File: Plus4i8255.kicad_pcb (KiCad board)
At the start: 2 copper layers, 52.1 x 70 mm, 13 parts, among them CN1 EXPANSION_PORT, CN3 PIN_HEADER_32PIN, U1 8255, U2 GAL20V8

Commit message: TurboFloppy -> Plus4i8255
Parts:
- CN1: footprint TurboFloppy:C16_Cart_Conn -> Plus4i8255:C16_Cart_Conn
- V0: footprint TurboFloppy:cc_by_nc_sa -> Plus4i8255:cc_by_nc_sa
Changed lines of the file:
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@@
 		(property ki_fp_filters "R?Array?SIP*")
 		(sheetname "Root")
-		(sheetfile "TurboFloppy.kicad_sch")
+		(sheetfile "Plus4i8255.kicad_sch")
 		(attr through_hole)
 		(fp_line
@@
 		(property ki_fp_filters "MountingHole*Pad*")
 		(sheetname "Root")
-		(sheetfile "TurboFloppy.kicad_sch")
+		(sheetfile "Plus4i8255.kicad_sch")
 		(zone_connect 2)
 		(attr exclude_from_pos_files exclude_from_bom)
@@
 		(property ki_fp_filters "DIP*W15.24mm* PDIP*W15.24mm*")
 		(sheetname "Root")
-		(sheetfile "TurboFloppy.kicad_sch")
+		(sheetfile "Plus4i8255.kicad_sch")
 		(attr through_hole)
 		(fp_line
@@
 		(property ki_fp_filters "R?Array?SIP*")
 		(sheetname "Root")
-		(sheetfile "TurboFloppy.kicad_sch")
+		(sheetfile "Plus4i8255.kicad_sch")
 		(attr through_hole)
 		(fp_line
@@
 		(property ki_fp_filters "MountingHole*Pad*")
 		(sheetname "Root")
-		(sheetfile "TurboFloppy.kicad_sch")
+		(sheetfile "Plus4i8255.kicad_sch")
 		(zone_connect 2)
 		(attr exclude_from_pos_files exclude_from_bom)
@@
 		(property ki_fp_filters "R?Array?SIP*")
 		(sheetname "Root")
-		(sheetfile "TurboFloppy.kicad_sch")
+		(sheetfile "Plus4i8255.kicad_sch")
 		(attr through_hole)
 		(fp_line
@@
 		(property ki_fp_filters "DIP* PDIP*")
 		(sheetname "Root")
-		(sheetfile "TurboFloppy.kicad_sch")
+		(sheetfile "Plus4i8255.kicad_sch")
 		(attr through_hole)
 		(fp_line
@@
 		(property ki_fp_filters "C_*")
 		(sheetname "Root")
-		(sheetfile "TurboFloppy.kicad_sch")
+		(sheetfile "Plus4i8255.kicad_sch")
 		(attr through_hole)
 		(fp_line
@@
 		(property ki_fp_filters "C_*")
 		(sheetname "Root")
-		(sheetfile "TurboFloppy.kicad_sch")
+		(sheetfile "Plus4i8255.kicad_sch")
 		(attr through_hole)
 		(fp_line
@@
 		)
 	)
-	(footprint "TurboFloppy:C16_Cart_Conn"
+	(footprint "Plus4i8255:C16_Cart_Conn"
 		(layer "F.Cu")
 		(at 146.053 132.588)
@@
 			)
 		)
-		(property "Footprint" "TurboFloppy:C16_Cart_Conn"
+		(property "Footprint" "Plus4i8255:C16_Cart_Conn"
 			(at 0 0 0)
 			(layer "F.Fab")
@@
 		)
 		(sheetname "Root")
-		(sheetfile "TurboFloppy.kicad_sch")
+		(sheetfile "Plus4i8255.kicad_sch")
 		(zone_connect 2)
 		(attr through_hole)
@@
 		(property ki_fp_filters "Connector*:*_2x??_*")
 		(sheetname "Root")
-		(sheetfile "TurboFloppy.kicad_sch")
+		(sheetfile "Plus4i8255.kicad_sch")
 		(attr through_hole)
 		(fp_line
@@
 		(property ki_fp_filters "CP_*")
 		(sheetname "Root")
-		(sheetfile "TurboFloppy.kicad_sch")
+		(sheetfile "Plus4i8255.kicad_sch")
 		(attr through_hole)
 		(fp_line
@@
 		)
 	)
-	(footprint "TurboFloppy:cc_by_nc_sa"
+	(footprint "Plus4i8255:cc_by_nc_sa"
 		(layer "B.Cu")
 		(at 161.925 125.222 180)
@@
 			)
 		)
-		(property "Footprint" "TurboFloppy:cc_by_nc_sa"
+		(property "Footprint" "Plus4i8255:cc_by_nc_sa"
 			(at 0 0 0)
 			(layer "B.Fab")
@@
 		)
 		(sheetname "Root")
-		(sheetfile "TurboFloppy.kicad_sch")
+		(sheetfile "Plus4i8255.kicad_sch")
 		(attr through_hole)
 		(fp_poly

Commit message: Add PC-style DB25 parallel port Inspired by zx_spectrum_parallel_interface by @msolajic TBD: Check DB25 footprint!
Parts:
- added C3: 100n, Capacitor_THT:C_Disc_D7.0mm_W2.5mm_P5.00mm, F.Cu at (135.9, 92.0)
- added CN2: PC_PARALLEL, Connector_Dsub:DSUB-25_Female_Horizontal_P2.77x2.84mm_EdgePinOffset7.70mm_Housed_MountingHolesOffset9.12mm, F.Cu at (129.4, 64.0)
- added JP1: JMP_PARPWR, Jumper:SolderJumper-2_P1.3mm_Open_RoundedPad1.0x1.5mm, B.Cu at (130.2, 58.5)
- added JP2: JMP_SELPRNT, Jumper:SolderJumper-2_P1.3mm_Open_RoundedPad1.0x1.5mm, B.Cu at (138.5, 58.5)
- added U3: 74HCT04, Package_DIP:DIP-14_W7.62mm_Socket_LongPads, F.Cu at (139.7, 98.3)
- renumbered C3 to C4
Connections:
- RN1 pad 2: /pb7 -> /pb5
- RN1 pad 4: /pb5 -> /pb7
- U2 pad 1: /~{reset} -> unconnected-(U2-I1-Pad1)
- U2 pad 17: /reset -> unconnected-(U2-IO17-Pad17)
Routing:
- net /~{strobe}: track 0.00 -> 69.6 mm, vias 0 -> 2
- net +5V: track 114.5 -> 166.5 mm, vias 1 -> 4
- net /pb7: track 59.6 -> 86.7 mm, vias 2 -> 3
- net /pc3: track 32.1 -> 55.8 mm, vias 0 -> 1
- net /pb6: track 61.5 -> 79.2 mm, vias 0 -> 1
- net /reset: track 25.3 -> 11.5 mm, vias 1 -> 0
- net /~{reset}: track 70.0 -> 82.0 mm, vias 2 -> 3
- net /pb0: track 13.0 -> 24.9 mm
- net /pb4: track 69.5 -> 81.3 mm, vias 1 -> 2
- net /pb1: track 19.7 -> 31.4 mm
- net /pb2: track 25.3 -> 36.9 mm
- net /pc7: track 36.0 -> 46.1 mm
- net /pb5: track 72.9 -> 82.4 mm, vias 2 -> 3
- net /pb3: track 50.6 -> 59.1 mm
- net /~{wr8255}: track 29.8 -> 34.6 mm
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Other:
- board size 52.1 x 70 mm -> 53.3 x 83.2 mm
- board text added: "PC-STYLE PARALLEL PORT"
- board text added: "PIN 14 +5V"
- board text added: "PIN 17 SELECT PRINTER"

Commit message: Move some tracks around
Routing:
- net /pb5: track 82.4 -> 79.4 mm
- net /~{rd8255}: track 43.6 -> 40.9 mm
- net /~{wr8255}: track 34.6 -> 32.2 mm
- net /a1: track 57.3 -> 58.8 mm
- net /a0: track 63.4 -> 63.9 mm

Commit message: Again
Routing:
- net /a0: track 63.9 -> 66.9 mm
- net /a1: track 58.8 -> 61.6 mm
- net /~{wr8255}: track 32.2 -> 34.9 mm, vias 1 -> 2
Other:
- outline, holes or cut-outs redrawn
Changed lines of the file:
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@@
 	(gr_line
 		(start 172.72 53.467)
-		(end 172.72 128.016)
+		(end 172.72 127.381)
 		(stroke
 			(width 0.05)
@@
 	(gr_line
 		(start 120.015 135.89)
-		(end 120.015 128.651)
+		(end 120.015 128.016)
 		(stroke
 			(width 0.05)
@@
 	)
 	(gr_arc
-		(start 172.72 128.016)
-		(mid 172.534013 128.465013)
-		(end 172.085 128.651)
+		(start 172.72 127.381)
+		(mid 172.534013 127.830013)
+		(end 172.085 128.016)
 		(stroke
 			(width 0.05)
@@
 	)
 	(gr_arc
-		(start 120.015 128.651)
-		(mid 119.565987 128.465013)
-		(end 119.38 128.016)
+		(start 120.015 128.016)
+		(mid 119.565987 127.830013)
+		(end 119.38 127.381)
 		(stroke
 			(width 0.05)
@@
 	(gr_line
 		(start 172.085 135.89)
-		(end 172.085 128.651)
+		(end 172.085 128.016)
 		(stroke
 			(width 0.05)
@@
 	)
 	(gr_line
-		(start 119.38 128.016)
+		(start 119.38 127.381)
 		(end 119.38 53.467)
 		(stroke
@@
 	)
 	(segment
-		(start 167.005 116.205)
+		(start 168.91 106.553)
 		(end 167.005 108.458)
 		(width 0.25)
@@
 	)
 	(segment
-		(start 149.86 86.868)
-		(end 151.129998 88.137998)
+		(start 167.005 108.458)
+		(end 167.005 116.205)
 		(width 0.25)
 		(layer "F.Cu")
@@
 	)
 	(segment
-		(start 168.91 106.553)
-		(end 168.91 100.33)
+		(start 149.86 86.868)
+		(end 149.86 88.392)
 		(width 0.25)
 		(layer "F.Cu")
@@
 	)
 	(segment
-		(start 167.005 108.458)
+		(start 168.91 95.25)
 		(end 168.91 106.553)
 		(width 0.25)
@@
 	)
 	(segment
-		(start 151.129998 88.137998)
+		(start 151.129998 89.661998)
 		(end 151.129998 95.25)
 		(width 0.25)
@@
 		(net 4)
 	)
+	(segment
+		(start 149.86 88.392)
+		(end 151.129998 89.661998)
+		(width 0.25)
+		(layer "F.Cu")
+		(net 4)
+	)
 	(via
 		(at 151.129998 95.25)
@@
 	)
 	(via
-		(at 168.91 100.33)
+		(at 168.91 95.25)
 		(size 0.6)
 		(drill 0.4)
@@
 	)
 	(segment
-		(start 168.91 100.33)
-		(end 160.782 100.33)
-		(width 0.25)
-		(layer "B.Cu")
-		(net 4)
-	)
-	(segment
-		(start 160.782 100.33)
-		(end 155.702 95.25)
-		(width 0.25)
-		(layer "B.Cu")
-		(net 4)
-	)
-	(segment
-		(start 155.702 95.25)
+		(start 168.91 95.25)
 		(end 151.129998 95.25)
 		(width 0.25)
@@
 	)
 	(segment
-		(start 153.669996 88.137996)
-		(end 153.669996 93.091)
-		(width 0.25)
-		(layer "F.Cu")
-		(net 11)
-	)
-	(segment
-		(start 152.4 86.868)
-		(end 153.669996 88.137996)
+		(start 166.37 115.569996)
+		(end 166.369996 115.57)
 		(width 0.25)
 		(layer "F.Cu")
@@
 	)
 	(segment
-		(start 153.67 93.091004)
-		(end 153.669996 93.091)
+		(start 166.37 94.615)
+		(end 166.37 115.569996)
 		(width 0.25)
 		(layer "F.Cu")
@@
 	)
 	(segment
-		(start 153.669996 93.091)
-		(end 153.669996 93.345)
+		(start 153.67 89.662)
+		(end 152.4 88.392)
 		(width 0.25)
 		(layer "F.Cu")
@@
 	(segment
 		(start 153.67 94.615)
-		(end 153.67 93.091004)
+		(end 153.67 89.662)
 		(width 0.25)
 		(layer "F.Cu")
@@
 	)
 	(segment
-		(start 166.37 99.695)
-		(end 166.37 115.569996)
-		(width 0.25)
-		(layer "F.Cu")
-		(net 11)
-	)
-	(segment
-		(start 166.37 115.569996)
-		(end 166.369996 115.57)
+		(start 152.4 88.392)
+		(end 152.4 86.868)
 		(width 0.25)
 		(layer "F.Cu")
@@
 	)
 	(via
-		(at 166.37 99.695)
+		(at 166.37 94.615)
 		(size 0.6)
 		(drill 0.4)
@@
 	)
 	(segment
-		(start 156.083 94.615)
-		(end 153.67 94.615)
-		(width 0.25)
-		(layer "B.Cu")
-		(net 11)
-	)
-	(segment
 		(start 160.053 132.588)
 		(end 160.053 121.886996)
@@
 	)
 	(segment
-		(start 166.37 99.695)
-		(end 161.163 99.695)
-		(width 0.25)
-		(layer "B.Cu")
-		(net 11)
-	)
-	(segment
-		(start 156.972 95.504)
-		(end 156.083 94.615)
-		(width 0.25)
-		(layer "B.Cu")
-		(net 11)
-	)
-	(segment
-		(start 161.163 99.695)
-		(end 156.972 95.504)
+		(start 160.053 121.886996)
+		(end 166.369996 115.57)
 		(width 0.25)
 		(layer "B.Cu")
@@
 	)
 	(segment
-		(start 160.053 121.886996)
-		(end 166.369996 115.57)
+		(start 166.37 94.615)
+		(end 153.67 94.615)
 		(width 0.25)
 		(layer "B.Cu")
@@
 	)
 	(segment
+		(start 160.02 95.885)
+		(end 160.02 102.108)
+		(width 0.25)
+		(layer "F.Cu")
+		(net 72)
+	)
+	(segment
 		(start 147.955 105.156)
 		(end 147.955 107.061)
@@
 		(net 72)
 	)
-	(segment
-		(start 146.05 95.885)
-		(end 155.448 95.885)
-		(width 0.25)
-		(layer "B.Cu")
-		(net 72)
-	)
-	(segment
-		(start 160.02 100.457)
-		(end 160.02 102.108)
-		(width 0.25)
-		(layer "B.Cu")
+	(via
+		(at 160.02 95.885)
+		(size 0.6)
+		(drill 0.4)
+		(layers "F.Cu" "B.Cu")
 		(net 72)
 	)
 	(segment
-		(start 155.448 95.885)
-		(end 160.02 100.457)
+		(start 146.05 95.885)
+		(end 160.02 95.885)
 		(width 0.25)
 		(layer "B.Cu")
@@
 		(width 0.25)
 		(layer "B.Cu")
-		(net 74)
-	)
-	(segment
-		(start 157.353 101.473)
-		(end 157.48 101.473)
-		(width 0.25)
-		(layer "B.Cu")

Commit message: Ready for V3
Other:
- board text added: "V3"
- board text removed: "V2"
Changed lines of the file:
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@@
 	(title_block
 		(title "Intel 8255 Interface for the Commodore 16, 116 and Plus/4")
-		(date "2024-08-08")
-		(rev "2git")
+		(date "2025-04-16")
+		(rev "3")
 		(company "SukkoPera")
 		(comment 1 "Based on the article published in Rádiótechnika 1988/12 by Ferenc Garay and Dr. János Rohonczy")
@@
 		)
 	)
-	(gr_text "V2"
+	(gr_text "V3"
 		(at 125.079762 127.889 0)
 		(layer "B.SilkS")

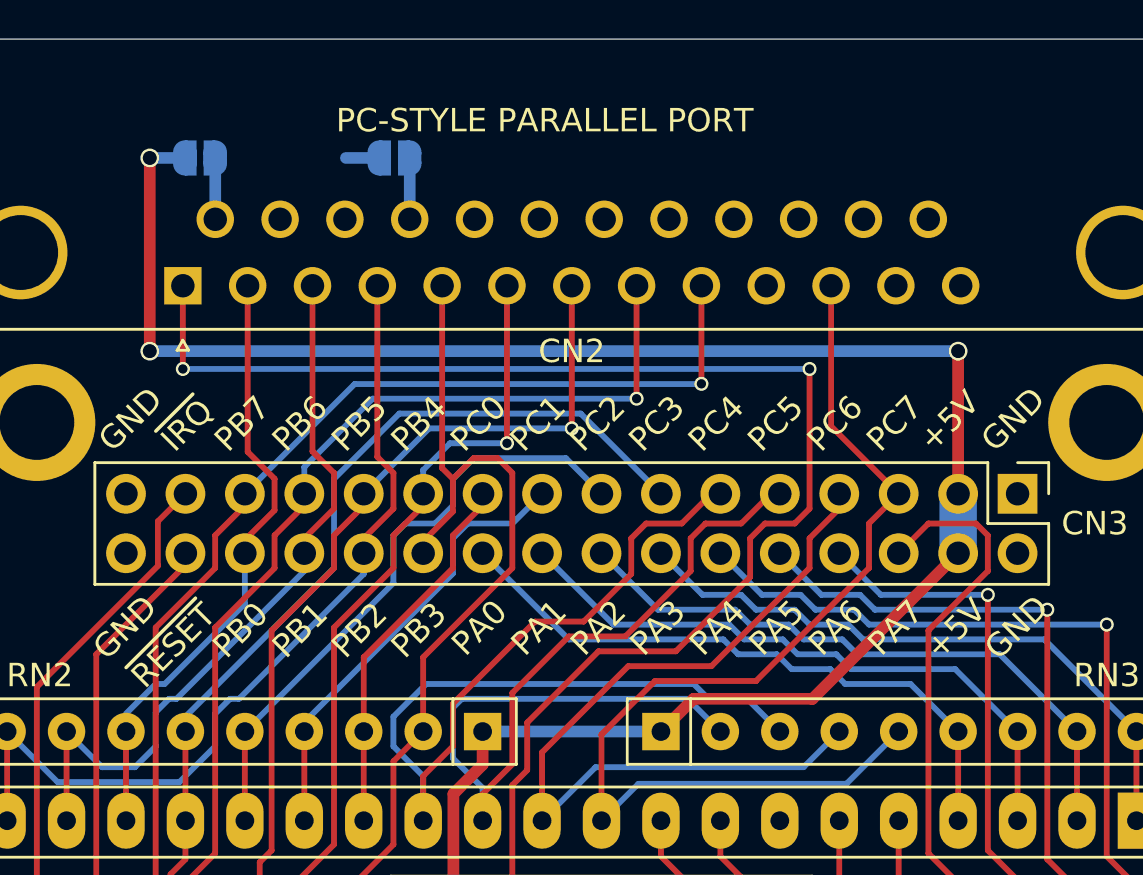
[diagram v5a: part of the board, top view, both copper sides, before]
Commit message: Change pins of PC-style parallel port, hopefully adding potential bidirectional capability
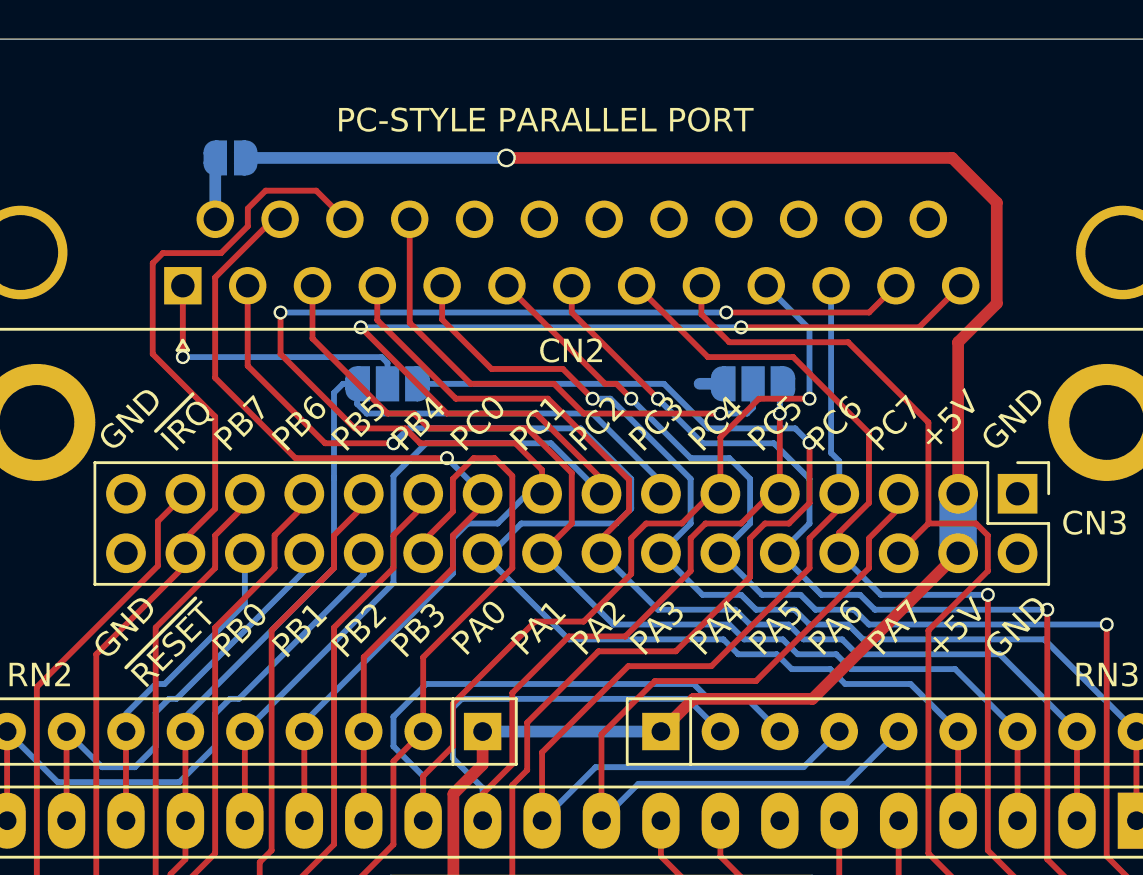
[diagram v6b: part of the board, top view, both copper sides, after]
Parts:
- added JP3: JMP_SELPRINT, Jumper:SolderJumper-3_P1.3mm_Open_RoundedPad1.0x1.5mm, B.Cu at (138.2, 68.2)
- JP2: value JMP_SELPRNT -> JMP_SELPRINT; footprint Jumper:SolderJumper-2_P1.3mm_Open_RoundedPad1.0x1.5mm -> Jumper:SolderJumper-3_P1.3mm_Open_RoundedPad1.0x1.5mm
- moved JP2 18.1 mm to (153.8, 68.2)
- moved JP1 1.30 mm to (131.5, 58.5), turned to 0 degrees
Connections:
- CN2 pad 10: unconnected-(CN2-Pad10) -> /pc4
- CN2 pad 11: /pc7 -> /pc6
- CN2 pad 12: unconnected-(CN2-Pad12) -> /pc1
- CN2 pad 13: unconnected-(CN2-Pad13) -> /pc2
- CN2 pad 15: unconnected-(CN2-P15-Pad15) -> /pc0
- CN2 pad 16: unconnected-(CN2-P16-Pad16) -> /~{reset}
- CN2 pad 2: /pb0 -> /pa0
- CN2 pad 3: /pb1 -> /pa1
- CN2 pad 4: /pb2 -> /pa2
- CN2 pad 5: /pb3 -> /pa3
- CN2 pad 6: /pb4 -> /pa4
- CN2 pad 7: /pb5 -> /pa5
- CN2 pad 8: /pb6 -> /pa6
- CN2 pad 9: /pb7 -> /pa7
- U3 pad 2: /~{strobe} -> Net-(JP3-B)
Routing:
- net /~{strobe}: track 69.6 -> 12.7 mm, vias 2 -> 1
- net Net-(JP3-B): track 0.00 -> 53.7 mm, vias 0 -> 1
- net /pc1: track 18.9 -> 61.7 mm, vias 0 -> 2
- net /pc2: track 26.4 -> 67.7 mm, vias 0 -> 2
- net /pa0: track 27.3 -> 58.0 mm, vias 0 -> 1
- net /pb7: track 86.7 -> 61.1 mm, vias 3 -> 2
- net /~{reset}: track 82.0 -> 106.4 mm
- net /pc0: track 15.6 -> 37.1 mm, vias 0 -> 1
- net /pb6: track 79.2 -> 57.8 mm, vias 1 -> 0
- net /pa1: track 27.3 -> 47.0 mm
- net Net-(CN2-P17): track 2.62 -> 21.8 mm, vias 0 -> 1
- net /pa2: track 27.3 -> 46.0 mm
- net /pa3: track 27.3 -> 45.9 mm, vias 0 -> 1
- net /pa6: track 36.3 -> 54.5 mm
- net /pa5: track 41.0 -> 59.0 mm, vias 1 -> 2
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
